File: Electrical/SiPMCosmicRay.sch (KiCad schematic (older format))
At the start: 14 parts

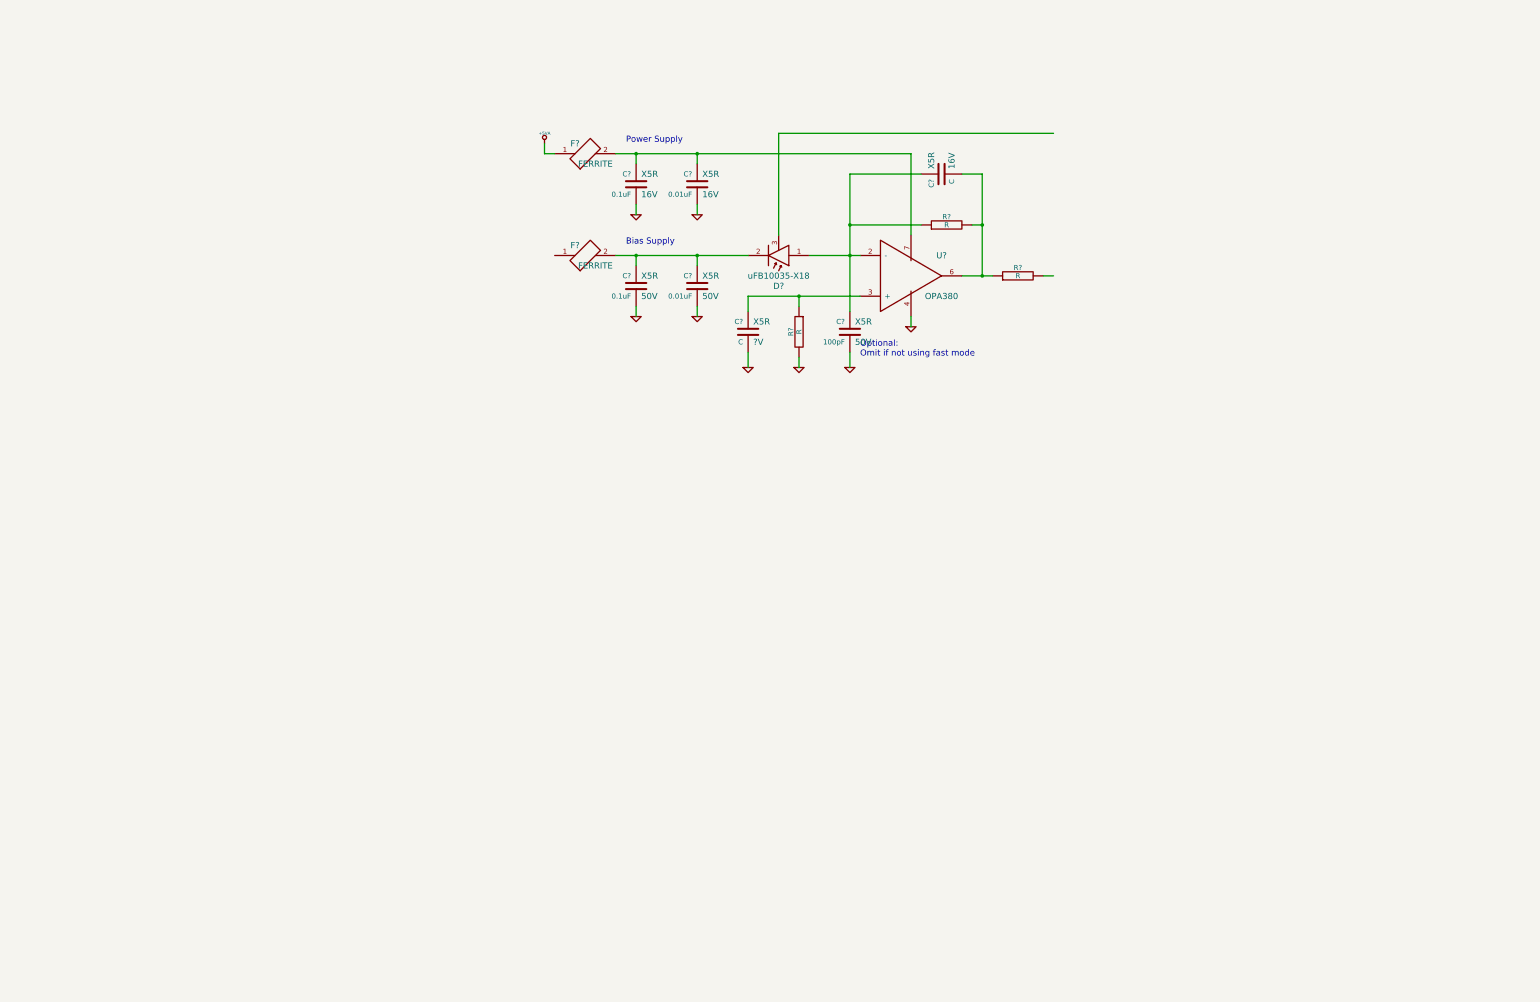
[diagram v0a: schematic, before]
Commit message: Added thermoelectric cooler controller to schematic
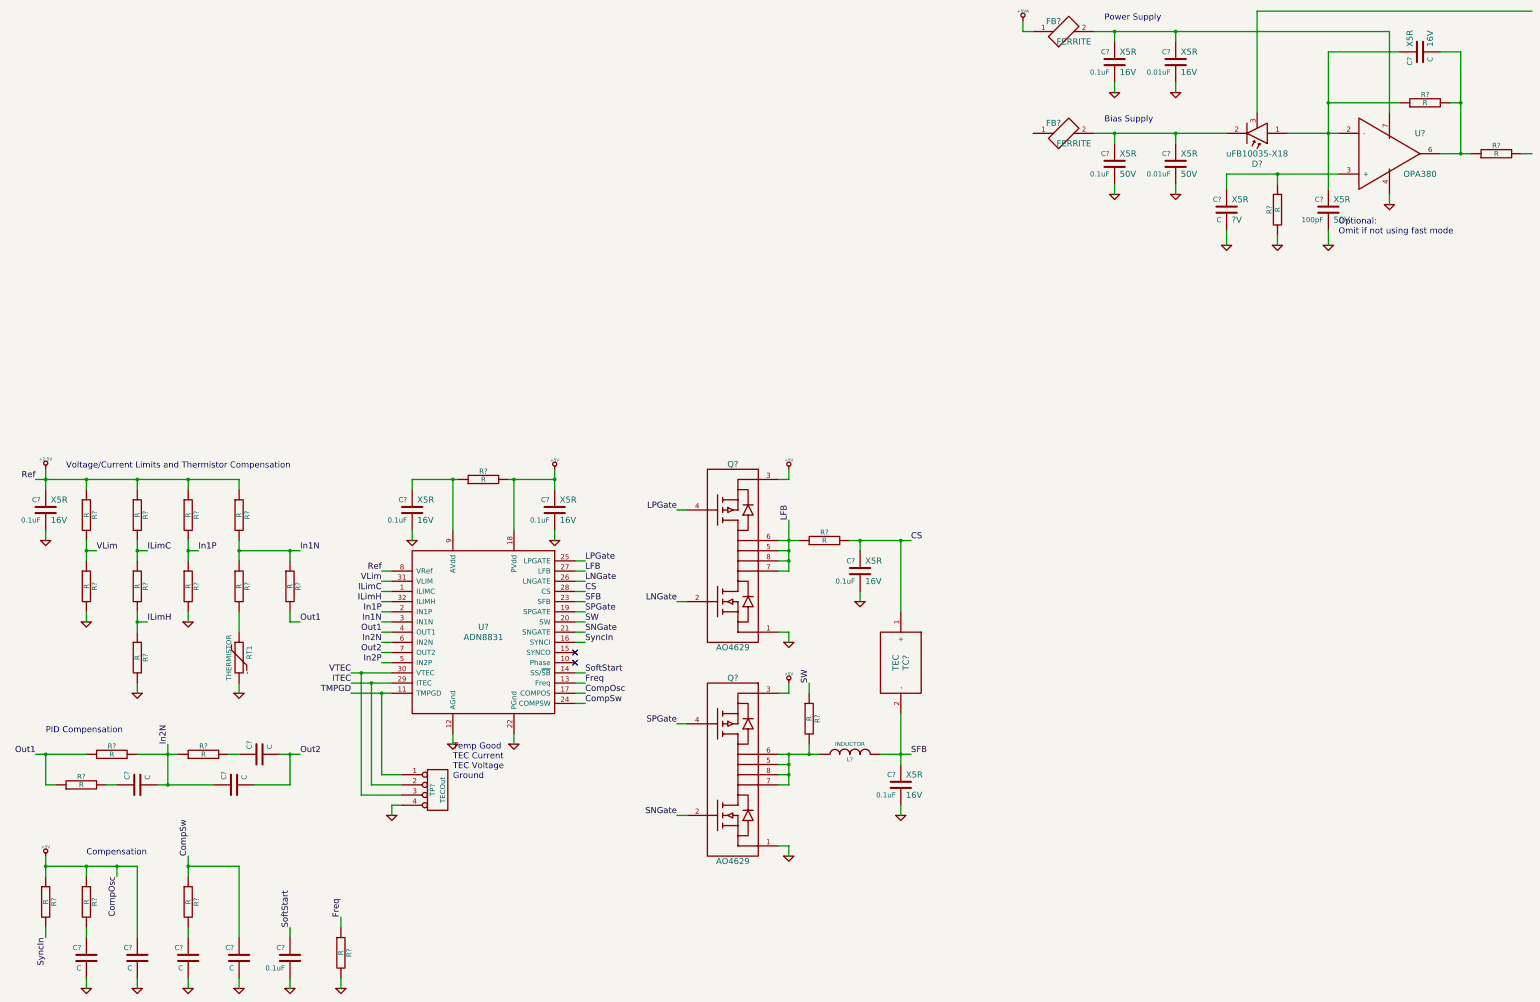
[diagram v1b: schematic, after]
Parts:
- removed F?: FERRITE, symbol FERRITE
- added C? (x6): 0.1uF, symbol C
- added C? (x7): C, symbol C
- added FB?: FERRITE, symbol FERRITE
- added L?: INDUCTOR, symbol INDUCTOR
- added Q? (x2): AO4629, symbol MOS_DUAL_PN
- added R? (x20): R, symbol R
- added RT1: THERMISTOR, symbol THERMISTOR
- added TC?: TEC, symbol TEC
- added TP?: TECOut, symbol CONN_4
- added U?: ADN8831, symbol ADN8831
- gave numbers to parts that had none: 1
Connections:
- net labels added: +2.5V, +5V, CS, CompOsc, CompSw, Freq, ILimC, ILimH, ITEC, In1N, In1P, In2N, In2P, LFB, LNGate, LPGate, Out1, Out2, Ref, SFB, SNGate, SPGate, SW, SoftStart, SyncIn, TMPGD, VLim, VTEC
- wire segments 31 -> 209
- no-connect marks 0 -> 2
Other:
- note added: "Compensation"
- note added: "PID Compensation"
- note added: "Temp Good\nTEC Current\nTEC Voltage\nGround"
- note added: "Voltage/Current Limits and Thermistor Compensation"
- moved on the sheet: C?, D?, FB?, R?, U?

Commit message: Broke schematic into hierarchal schematics
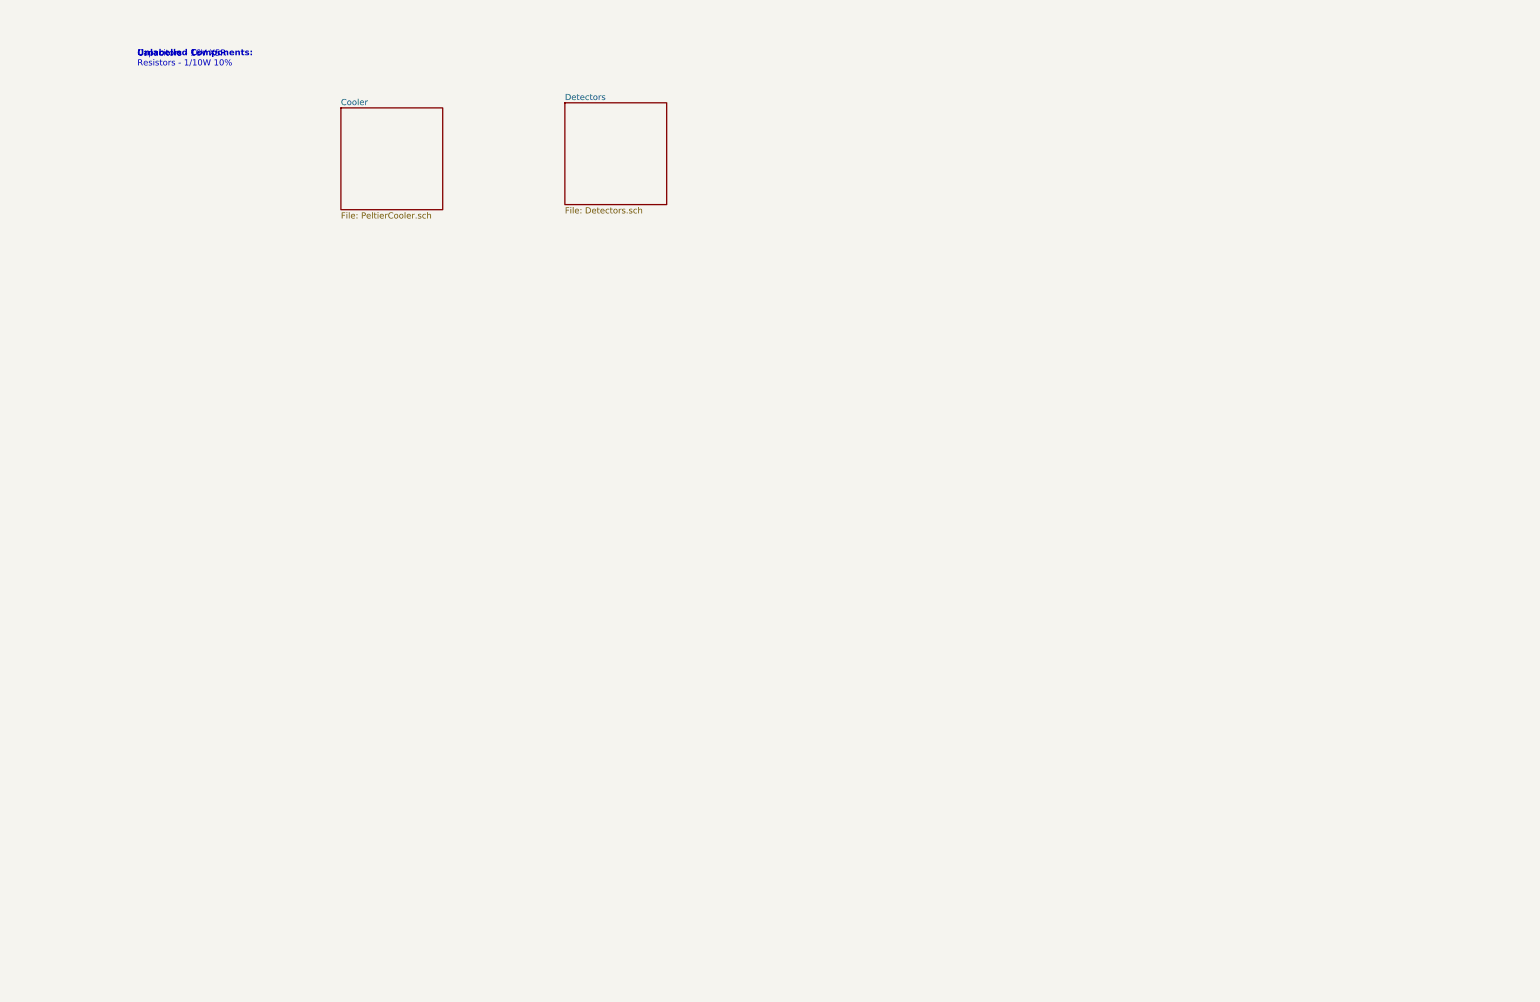
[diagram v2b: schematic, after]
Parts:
- removed C? (x8): 0.1uF, symbol C
- removed C? (x2): 0.01uF, symbol C
- removed C?: 100pF, symbol C
- removed C? (x9): C, symbol C
- removed D?: uFB10035-X18, symbol PHOTODIODE
- removed FB? (x2): FERRITE, symbol FERRITE
- removed L?: INDUCTOR, symbol INDUCTOR
- removed Q? (x2): AO4629, symbol MOS_DUAL_PN
- removed R? (x23): R, symbol R
- removed RT1: THERMISTOR, symbol THERMISTOR
- removed TC?: TEC, symbol TEC
- removed TP?: TECOut, symbol CONN_4
- removed U?: OPA380, symbol OPA381
- removed U?: ADN8831, symbol ADN8831
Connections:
- no-connect marks 2 -> 0
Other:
- note added: "Capacitors - 16V X5R\nResistors - 1/10W 10%"
- note added: "Unlabelled Components:"
- note removed: "Bias Supply"
- note removed: "Compensation"
- note removed: "Optional:\nOmit if not using fast mode"
- note removed: "PID Compensation"
- note removed: "Power Supply"
- note removed: "Temp Good\nTEC Current\nTEC Voltage\nGround"
- note removed: "Voltage/Current Limits and Thermistor Compensation"

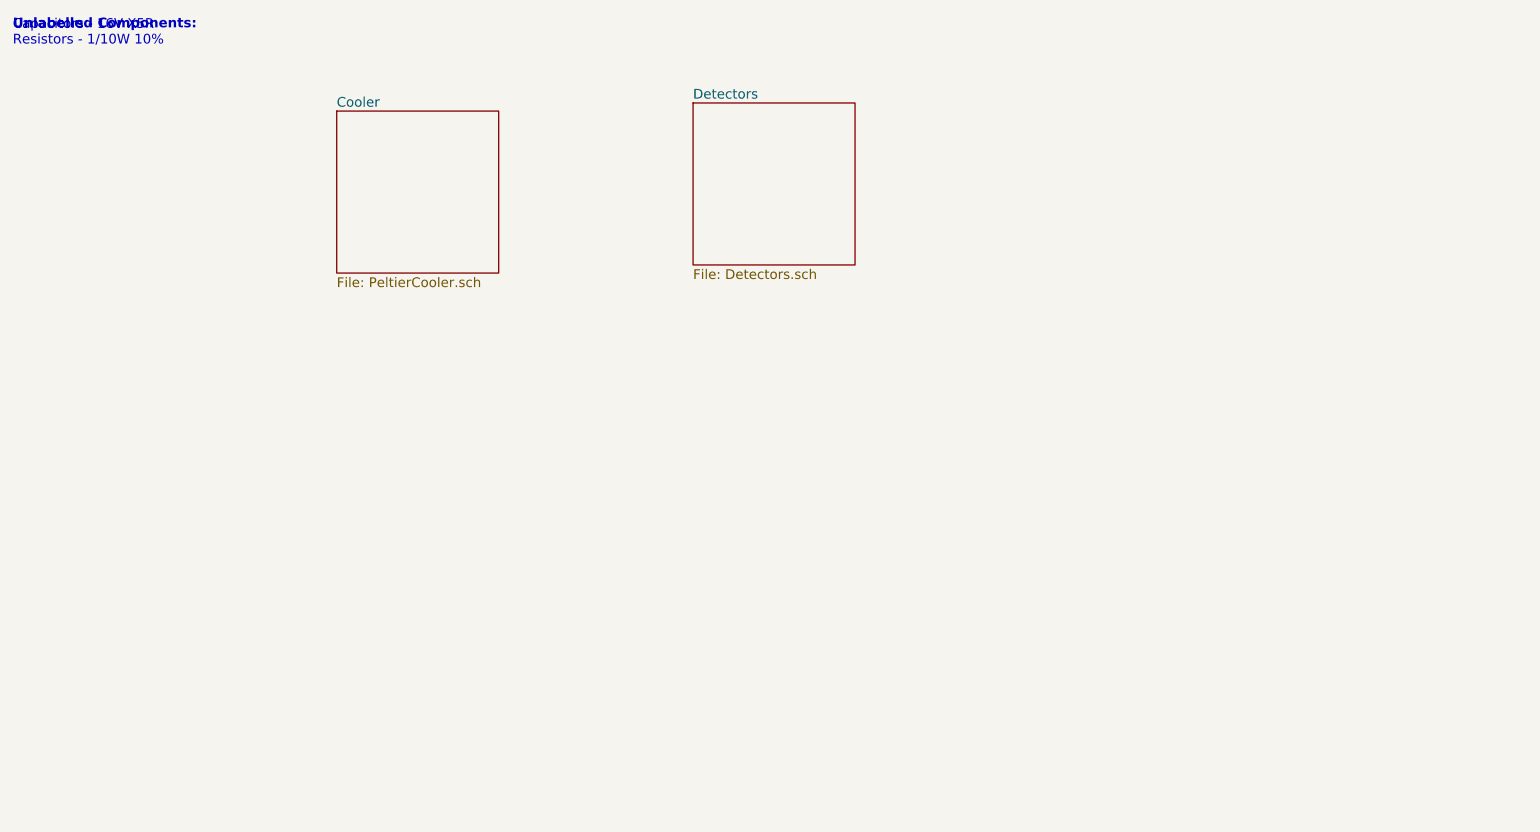
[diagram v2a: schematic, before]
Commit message: Added bias supply to schematic
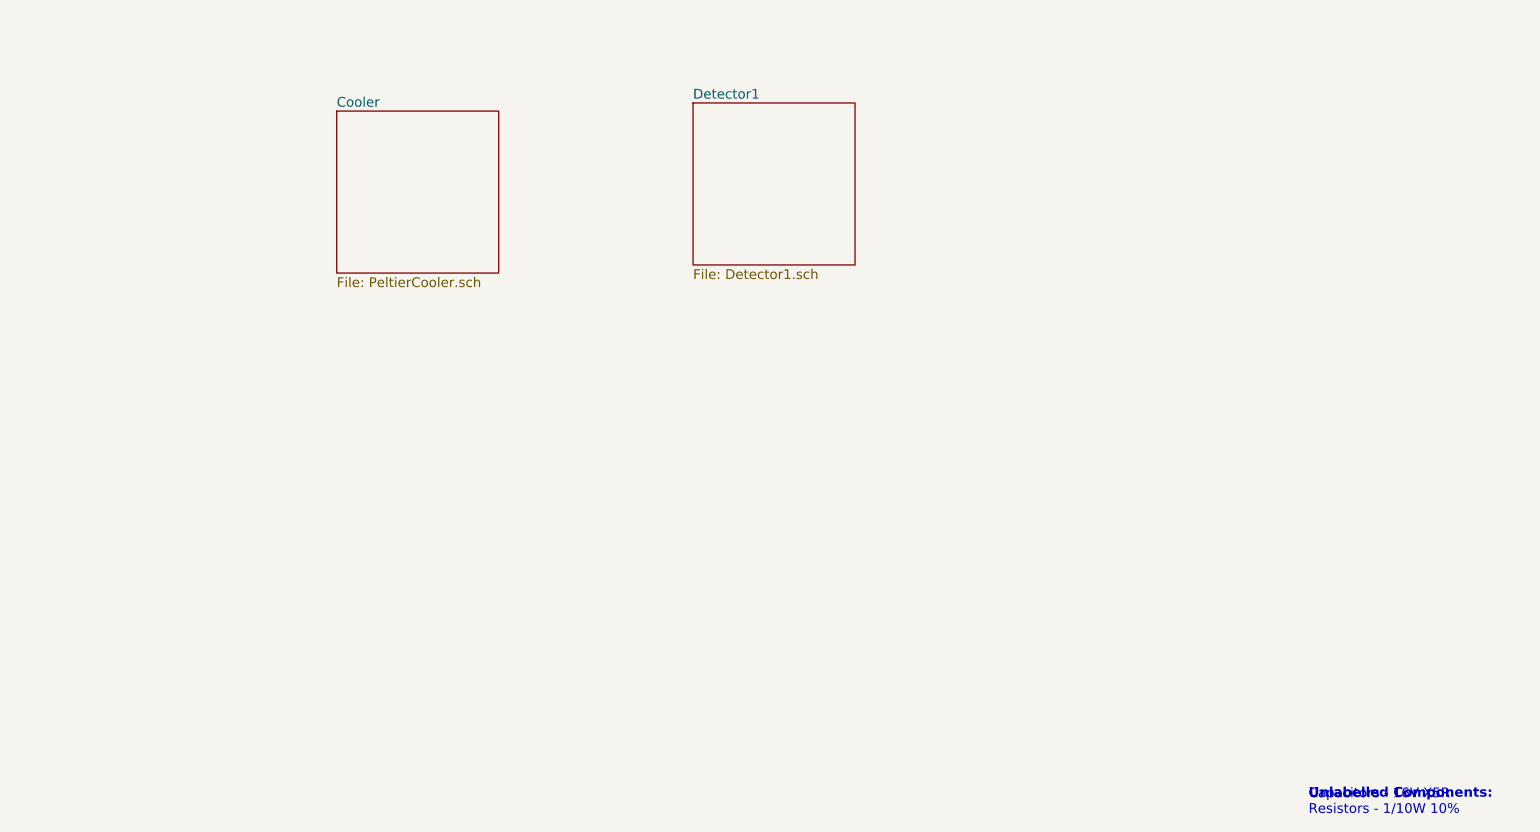
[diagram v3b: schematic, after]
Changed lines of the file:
@@
-EESchema Schematic File Version 2  date 4/14/2013 10:33:29 PM
+EESchema Schematic File Version 2  date 4/15/2013 12:10:38 AM
 LIBS:power
 LIBS:device
@@
 S 6100 2100 1000 1000
 U 516B74CB
-F0 "Detectors" 60
-F1 "Detectors.sch" 60
+F0 "Detector1" 60
+F1 "Detector1.sch" 60
 $EndSheet
 $Sheet
@@
 F1 "PeltierCooler.sch" 60
 $EndSheet
-Text Notes 1900 1650 0    60   ~ 12
+Text Notes 9900 6400 0    60   ~ 12
 Unlabelled Components:
-Text Notes 1900 1750 0    60   ~ 0
+Text Notes 9900 6500 0    60   ~ 0
 Capacitors - 16V X5R\nResistors - 1/10W 10%
 $EndSCHEMATC
